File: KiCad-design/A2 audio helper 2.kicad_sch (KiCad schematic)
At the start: 35 parts, among them J1 PIN HEADER 1x2, J10 PIN HEADER 1x2, J2 AudioJack3_Ground_Switch, J3 AudioJack3_Ground_Switch, J4 AudioJack3_Ground, J5 PIN HEADER 1x2, J6 PIN HEADER 1x4, J7 PIN HEADER 1x2, J8 PIN HEADER 1x3, J9 PIN HEADER 1x3, K1 Relay_DPDT, SW2 SW_DPDT_x2, U1 pam8403

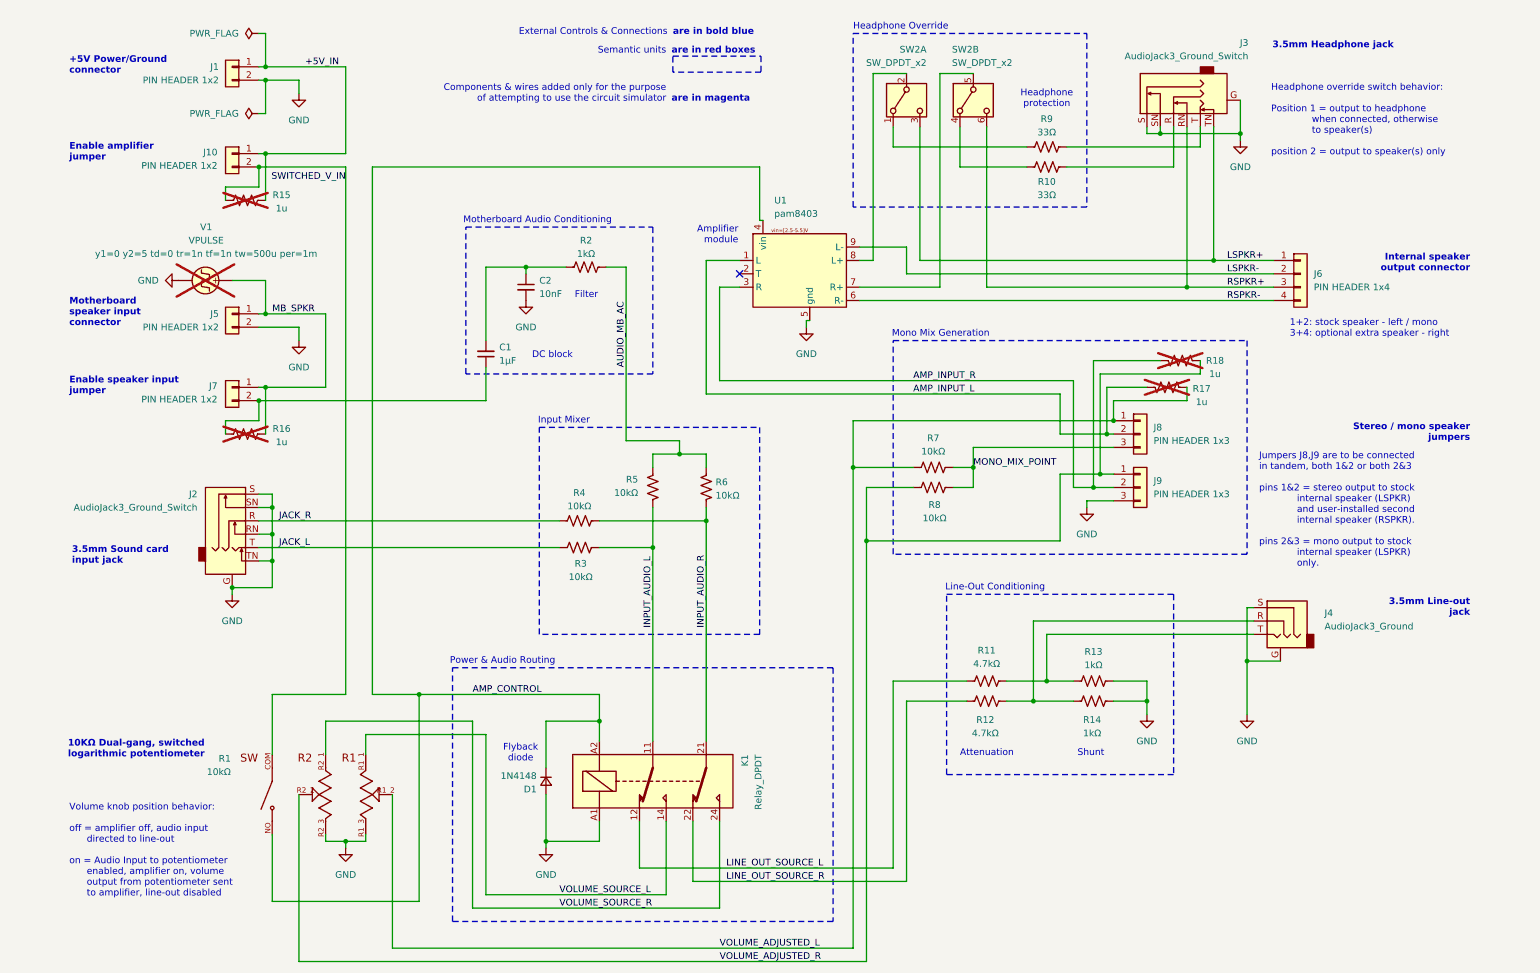
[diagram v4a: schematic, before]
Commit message: added 5V smoothing cap, added rear hp jack connector
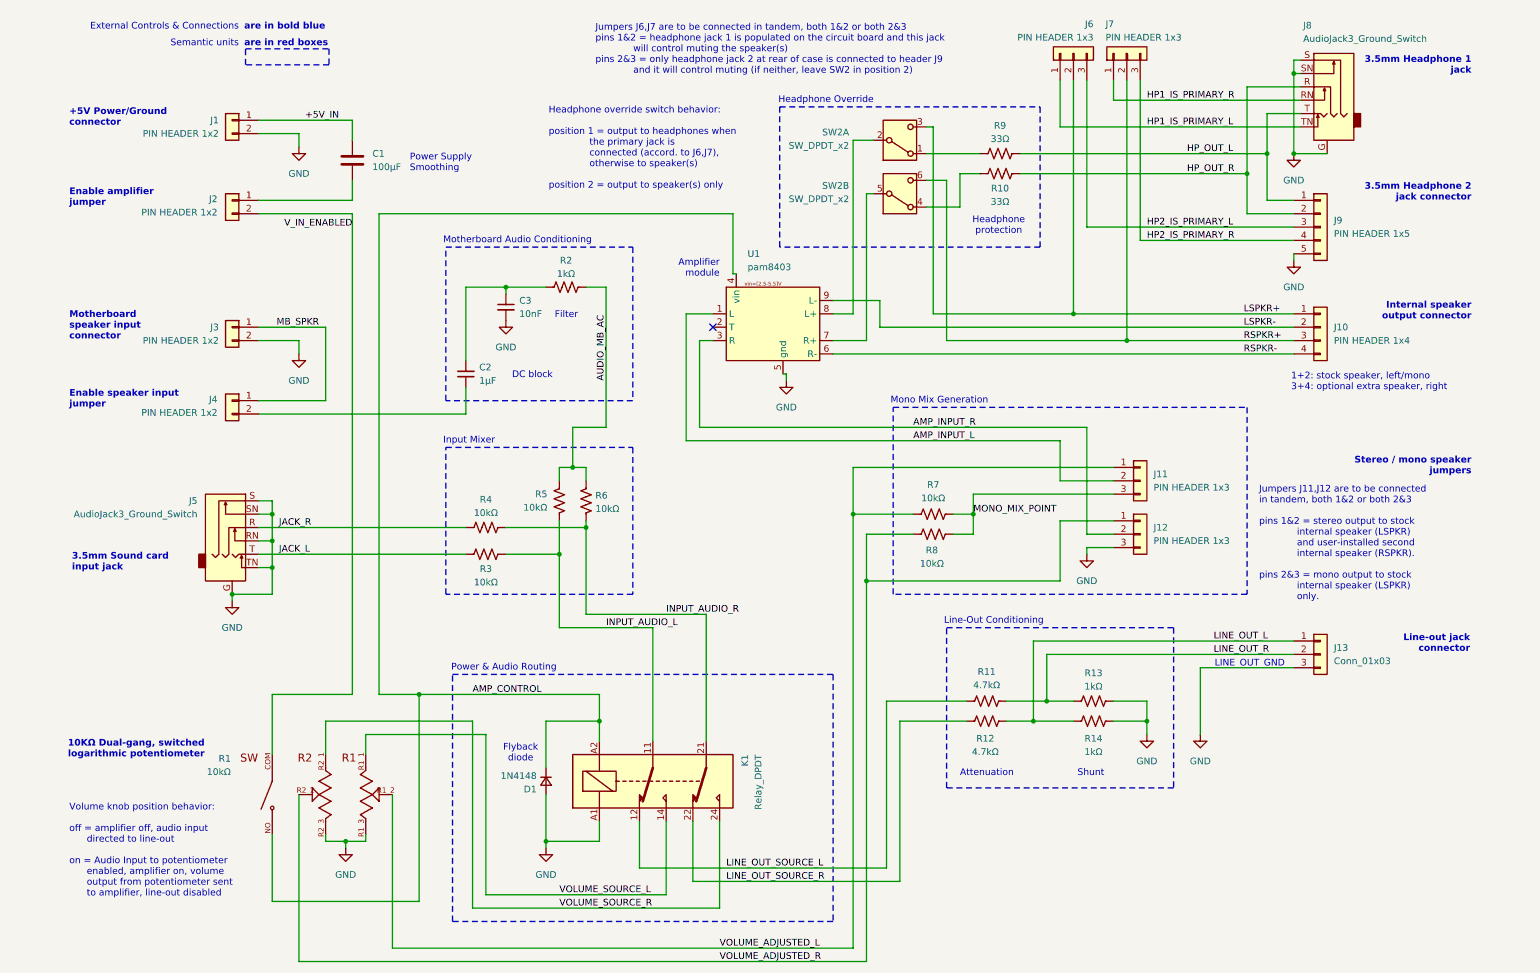
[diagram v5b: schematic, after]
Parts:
- removed J4: AudioJack3_Ground, symbol Connector_Audio:AudioJack3_Ground
- removed R15, R16, R17, R18: 1u, symbol Device:R_US
- removed V1: VPULSE, symbol Simulation_SPICE:VPULSE
- added C1: 100µF, symbol Device:C
- added J13: Conn_01x03, symbol Connector_Generic:Conn_01x03
- added J6, J7: PIN HEADER 1x3, symbol Connector_Generic:Conn_01x03
- added J9: PIN HEADER 1x5, symbol Connector_Generic:Conn_01x05
- renumbered C1 to C2, C2 to C3, J6 to J10, J8 to J11, J9 to J12, J10 to J2, J5 to J3, J7 to J4, J2 to J5, J3 to J8
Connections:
- net +5V_IN: now also C1.1; no longer J2.1 (Pin_1)
- net GND: now also J13.3 (Pin_3), J9.5 (Pin_5)
- net LSPKR+: now also J6.2 (Pin_2); no longer J8.TN
- net RSPKR+: now also J7.2 (Pin_2); no longer J8.RN
- net LINE_OUT_L: now reaches R12.1, R14.1
- net LINE_OUT_L: now also J13.1 (Pin_1)
- net HP_OUT_R: now reaches J8.R, R10.2
- net HP_OUT_R: now also J9.2 (Pin_2)
- net HP_OUT_L: now reaches J8.T, R9.2
- net HP_OUT_L: now also J9.1 (Pin_1)
- net LINE_OUT_R: now reaches R11.2, R13.1
- net LINE_OUT_R: now also J13.2 (Pin_2)
- net SWITCHED_V_IN renamed V_IN_ENABLED
- new net: C1.2, J2.1 (Pin_1)
- new net HP1_IS_PRIMARY_L: J6.1 (Pin_1), J8.TN
- new net HP1_IS_PRIMARY_R: J7.1 (Pin_1), J8.RN
- new net HP2_IS_PRIMARY_L: J6.3 (Pin_3), J9.3 (Pin_3)
- new net HP2_IS_PRIMARY_R: J7.3 (Pin_3), J9.4 (Pin_4)
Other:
- note added: "1+2: stock speaker, left/mono 3+4: optional extra speaker, right"
- note added: "3.5mm Headphone 1 jack"
- note added: "3.5mm Headphone 2 jack connector"
- note added: "Headphone override switch behavior: position 1 = output to headphones when the primary jack is connected (accord. to J6,J7), otherwise to speaker(s) position 2 = output to speaker(s) only"
- note added: "Jumpers J11,J12 are to be connected in tandem, both 1&2 or both 2&3 pins 1&2 = stereo output to stock internal speaker (LSPKR) and user-installed second internal speaker (RSPKR). pins 2&3 = mono output to stock internal speaker (LSPKR) only."
- note added: "Jumpers J6,J7 are to be connected in tandem, both 1&2 or both 2&3 pins 1&2 = headphone jack 1 is populated on the circuit board and this jack will control muting the speaker(s) pins 2&3 = only headphone jack 2 at rear of case is connected to header J9 and it will control muting (if neither, leave SW2 in position 2)"
- note added: "LINE_OUT_GND"
- note added: "Line-out jack connector"
- note added: "Power Supply Smoothing"
- note removed: "1+2: stock speaker - left / mono 3+4: optional extra speaker - right"
- note removed: "3.5mm Headphone jack"
- note removed: "3.5mm Line-out jack"
- note removed: "Components & wires added only for the purpose of attempting to use the circuit simulator"
- note removed: "Headphone override switch behavior: Position 1 = output to headphone when connected, otherwise to speaker(s) position 2 = output to speaker(s) only"
- note removed: "Jumpers J8,J9 are to be connected in tandem, both 1&2 or both 2&3 pins 1&2 = stereo output to stock internal speaker (LSPKR) and user-installed second internal speaker (RSPKR). pins 2&3 = mono output to stock internal speaker (LSPKR) only."
- note removed: "are in magenta"
- moved on the sheet: C2, C3, J1, J10, J11, J12, J2, J3, J4, J5, J8, R10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

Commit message: syms/footprints, 1st draft pcb
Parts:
- removed J5, J8: AudioJack3_Ground_Switch, symbol Connector_Audio:AudioJack3_Ground_Switch
- removed K1: Relay_DPDT, symbol Relay:Relay_DPDT
- added J5, J8: SJ1-3515N, SJ1-3515N:CUI_SJ1-3515N, symbol SJ1-3515N:SJ1-3515N
- added K1: SR11-5V-200-2C, SR11-5V-200-2C:RELAY_SR11-5V-200-2C, symbol SR11-5V-200-2C:SR11-5V-200-2C
- C1: footprint (none) -> Capacitor_THT:C_Radial_D6.3mm_H7.0mm_P2.50mm
- C2: footprint (none) -> Capacitor_THT:C_Radial_D5.0mm_H5.0mm_P2.00mm
- C3: footprint (none) -> Capacitor_THT:C_Disc_D4.7mm_W2.5mm_P5.00mm
- D1: footprint (none) -> Diode_THT:D_DO-35_SOD27_P7.62mm_Horizontal
- J1: footprint (none) -> Connector_Molex:Molex_KK-254_AE-6410-02A_1x02_P2.54mm_Vertical
- J10: footprint (none) -> Connector_PinHeader_2.54mm:PinHeader_1x04_P2.54mm_Horizontal
- J11, J12, J6, J7: footprint (none) -> Connector_PinHeader_2.54mm:PinHeader_1x03_P2.54mm_Vertical
- J13: value Conn_01x03 -> PIN HEADER 1x3; footprint (none) -> Connector_PinHeader_2.54mm:PinHeader_1x03_P2.54mm_Horizontal
- J2, J3, J4: footprint (none) -> Connector_PinHeader_2.54mm:PinHeader_1x02_P2.54mm_Vertical
- J9: footprint (none) -> Connector_PinHeader_2.54mm:PinHeader_1x05_P2.54mm_Horizontal
- R10, R11, R12, R13, R14, R2, R3, R4, R5, R6, R7, R8, R9: footprint (none) -> Resistor_THT:R_Axial_DIN0207_L6.3mm_D2.5mm_P10.16mm_Horizontal
- SW2: footprint (none) -> Button_Switch_THT:SW_CK_JS202011AQN_DPDT_Angled
- U1: footprint (none) -> pam8403:pam8403
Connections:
- net AMP_CONTROL: now also K1.A1
- net GND: now also J5.1, J5.4, J5.5, J8.1, K1.A2
- net HP1_IS_PRIMARY_L: now also J8.2
- net HP1_IS_PRIMARY_R: now also J8.3
- net HP_OUT_L: now also J8.4
- net HP_OUT_R: now also J8.5
- net INPUT_AUDIO_L: now also K1.COM1
- net INPUT_AUDIO_R: now also K1.COM2
- net JACK_L: now also J5.2
- net JACK_R: now also J5.3
- net LINE_OUT_SOURCE_L: now also K1.NC1
- net LINE_OUT_SOURCE_R: now also K1.NC2
- net VOLUME_SOURCE_L: now also K1.NO1
- net VOLUME_SOURCE_R: now also K1.NO2
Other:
- note added: "1+2: left / mono to stock speaker 3+4: right"
- note added: "Jumpers J11,J12 are to be connected in tandem, both 1&2 or both 2&3"
- note added: "pins 1&2 = (normal) stereo output, for stock internal speaker only, connect to LSPKR for left channel, RSPKR for right."
- note added: "pins 2&3 = mono output to stock int. speaker connected to LSPKR, however headphones will be mono also."
- note removed: "1+2: stock speaker, left/mono 3+4: optional extra speaker, right"
- note removed: "Jumpers J11,J12 are to be connected in tandem, both 1&2 or both 2&3 pins 1&2 = stereo output to stock internal speaker (LSPKR) and user-installed second internal speaker (RSPKR). pins 2&3 = mono output to stock internal speaker (LSPKR) only."
- moved on the sheet: D1, R3, R4

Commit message: minor simplification, 1st draft pcb
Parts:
- removed J4: PIN HEADER 1x2, Connector_PinHeader_2.54mm:PinHeader_1x02_P2.54mm_Vertical, symbol Connector_Generic:Conn_01x02
- J3: footprint Connector_PinHeader_2.54mm:PinHeader_1x02_P2.54mm_Vertical -> Connector_PinHeader_2.54mm:PinHeader_1x02_P2.54mm_Horizontal
- SW2: footprint Button_Switch_THT:SW_CK_JS202011AQN_DPDT_Angled -> Button_Switch_THT:SW_CK_JS202011CQN_DPDT_Straight
- renumbered J11 to J10, J12 to J11, J13 to J12, J10 to J19, J5 to J4, J6 to J5, J7 to J6, J8 to J7
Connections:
- net MB_SPKR: now also C2.1
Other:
- note added: "Jumpers J10,J11 are to be connected in tandem, both 1&2 or both 2&3"
- note added: "Jumpers J5,J6 are to be connected in tandem, both 1&2 or both 2&3 pins 1&2 = headphone jack 1 is populated on the circuit board and this jack will control muting the speaker(s) pins 2&3 = only headphone jack 2 at rear of case is connected to header J9 and it will control muting (if neither, leave SW2 in position 2)"
- note removed: "Enable speaker input jumper"
- note removed: "Jumpers J11,J12 are to be connected in tandem, both 1&2 or both 2&3"
- note removed: "Jumpers J6,J7 are to be connected in tandem, both 1&2 or both 2&3 pins 1&2 = headphone jack 1 is populated on the circuit board and this jack will control muting the speaker(s) pins 2&3 = only headphone jack 2 at rear of case is connected to header J9 and it will control muting (if neither, leave SW2 in position 2)"
- moved on the sheet: C2, C3, J3
